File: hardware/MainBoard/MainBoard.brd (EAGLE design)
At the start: 90 x 56 mm, 265 parts, among them J1 CON-71741-2184-BOT, J2 CON-71741-2184-TOP, J3 CON-FTSH-105-01-L-DV-K, J4 CON-ZX62R-B-5P, J7 CON-RJ45-J0G-0007NL, J8 SWITCH-CJS-1200-1200, M1 MOUNT-HOLE3.3, M2 MOUNT-HOLE3.3, M3 MOUNT-HOLE3.3, M4 MOUNT-HOLE3.3, M5 FIDUCIAL1X2, M6 FIDUCIAL1X2, M7 FIDUCIAL1X2, M8 FIDUCIAL1X2, Q1 MMBT3904, SW1 SWITCH-ESWITCH-TL3340G, SW2 SWITCH-ESWITCH-TL3340G, U1 A2F500M3G-1FGG256, U2 MAX19706-T4877-4, U3 MAX19706-T4877-4, U4 USBLC6-2SC6, U5 FT232HL, U6 DP83848C-VBH48A, U7 93LC56BT-OT, U8 DS1818-10-SOT-23, X1 ECX-2236-200, X2 ECX-31B, X3 ASEM1-C, X5 ECX-42-120

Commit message: Minor cleanup and markup on schematic and board.
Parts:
- turned X5 to 90 degrees
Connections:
- net UXCSI: now also X5.3; no longer X5.1
- net UXCSO: now also X5.1; no longer X5.3
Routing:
- net DGND: track 148.5 -> 143.7 mm, vias 77 -> 75
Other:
- board text added: "Add more vias"
- board text added: "Consider adding thermal vias"
- board text added: "JTAG"
- board text added: "Reroute JTAG signals"
- board text added: "Star topology for ETH, USB, SF, AFEs?"
- board text removed: "Redraw JTAG signals"
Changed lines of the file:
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@@
 <setting verticaltext="up"/>
 </settings>
-<grid distance="100" unitdist="mil" unit="mil" style="lines" multiple="1" display="yes" altdistance="25" altunitdist="mil" altunit="mil"/>
+<grid distance="1" unitdist="mm" unit="mm" style="lines" multiple="1" display="yes" altdistance="0.25" altunitdist="mm" altunit="mm"/>
 <layers>
 <layer number="1" name="Top" color="4" fill="1" visible="yes" active="yes"/>
@@
 <layer number="14" name="Inner2" color="10" fill="6" visible="no" active="yes"/>
 <layer number="15" name="D3V3" color="4" fill="6" visible="no" active="yes"/>
-<layer number="16" name="Bottom" color="1" fill="1" visible="yes" active="yes"/>
+<layer number="16" name="Bottom" color="1" fill="1" visible="no" active="yes"/>
 <layer number="17" name="Pads" color="2" fill="1" visible="yes" active="yes"/>
 <layer number="18" name="Vias" color="2" fill="1" visible="yes" active="yes"/>
@@
 <rectangle x1="23" y1="6" x2="28" y2="8" layer="101"/>
 <rectangle x1="25" y1="32" x2="36" y2="42" layer="101"/>
-<text x="25" y="31" size="0.4064" layer="101">Should USB data signals run in the same layer?</text>
+<text x="20" y="31" size="0.8128" layer="101">Should USB data signals run in the same layer?</text>
 <rectangle x1="10" y1="25" x2="17" y2="33" layer="101"/>
-<text x="9" y="25" size="0.8128" layer="101" rot="R90">Redraw JTAG signals</text>
+<text x="8" y="24" size="0.8128" layer="101">Reroute JTAG signals</text>
 <text x="8.5" y="18.25" size="1.27" layer="21" font="vector" rot="R90">RESET</text>
 <text x="8.5" y="12.25" size="1.27" layer="21" font="vector" rot="R90">USER</text>
@@
 <text x="91.98" y="18.62" size="0.8128" layer="101" rot="R90">Should planes be closer to board edge?</text>
 <text x="-0.73" y="13.54" size="0.8128" layer="101" rot="R90">-moving the FTSH header 0.5 mm north</text>
+<text x="12" y="28.75" size="1.27" layer="21" font="vector" rot="R90">JTAG</text>
+<text x="40.54" y="17.73" size="0.8128" layer="101">Consider adding thermal vias</text>
+<rectangle x1="35" y1="16" x2="43" y2="24" layer="101"/>
+<rectangle x1="51" y1="16" x2="59" y2="24" layer="101"/>
+<text x="23.54" y="12.73" size="0.8128" layer="101">Add more vias</text>
+<text x="23.54" y="11.73" size="0.8128" layer="101">Star topology for ETH, USB, SF, AFEs?</text>
 </plain>
 <attributes>
@@
 <attribute name="TOLERANCE" value="1%" x="19" y="38.25" size="1.778" layer="28" rot="MR0" display="off"/>
 </element>
-<element name="X5" library="MainBoard" package="ECX-42" value="ECX-42-120" x="12.5" y="40.5" rot="R270">
-<attribute name="CLOAD" value="9 pF" x="12.5" y="40.5" size="1.778" layer="27" rot="R270" display="off"/>
-<attribute name="DIGI-KEY#" value="XC1608CT-ND" x="12.5" y="40.5" size="1.778" layer="27" rot="R270" display="off"/>
-<attribute name="FREQ-TOLERANCE" value="10 ppm" x="12.5" y="40.5" size="1.778" layer="27" rot="R270" display="off"/>
-<attribute name="MPN" value="ECS-120-9-42-CKM-TR" x="12.5" y="40.5" size="1.778" layer="27" rot="R270" display="off"/>
-<attribute name="FREQ-STABILITY" value="10 ppm" x="12.5" y="40.5" size="1.778" layer="27" rot="R270" display="off"/>
-<attribute name="MF" value="ECS" x="12.5" y="40.5" size="1.778" layer="27" rot="R270" display="off"/>
+<element name="X5" library="MainBoard" package="ECX-42" value="ECX-42-120" x="12.5" y="40.5" rot="R90">
+<attribute name="CLOAD" value="9 pF" x="12.5" y="40.5" size="1.778" layer="27" rot="R90" display="off"/>
+<attribute name="DIGI-KEY#" value="XC1608CT-ND" x="12.5" y="40.5" size="1.778" layer="27" rot="R90" display="off"/>
+<attribute name="FREQ-TOLERANCE" value="10 ppm" x="12.5" y="40.5" size="1.778" layer="27" rot="R90" display="off"/>
+<attribute name="MPN" value="ECS-120-9-42-CKM-TR" x="12.5" y="40.5" size="1.778" layer="27" rot="R90" display="off"/>
+<attribute name="FREQ-STABILITY" value="10 ppm" x="12.5" y="40.5" size="1.778" layer="27" rot="R90" display="off"/>
+<attribute name="MF" value="ECS" x="12.5" y="40.5" size="1.778" layer="27" rot="R90" display="off"/>
 </element>
 <element name="C71" library="MainBoard" package="C0402" value="10pF" x="12.5" y="37" rot="R180"/>
@@
 <contactref element="C103" pad="2"/>
 <contactref element="C104" pad="2"/>
-<contactref element="C72" pad="2"/>
-<contactref element="C71" pad="2"/>
 <contactref element="C105" pad="2"/>
 <contactref element="C106" pad="2"/>
@@
 <vertex x="87" y="53"/>
 </polygon>
-<wire x1="10" y1="39.85" x2="10" y2="39" width="0.3048" layer="1"/>
-<via x="10" y="39" extent="1-16" drill="0.2032"/>
-<wire x1="11.7" y1="39" x2="10" y2="39" width="0.3048" layer="1"/>
-<wire x1="11.85" y1="37" x2="11" y2="37" width="0.3048" layer="1"/>
-<via x="11" y="37" extent="1-16" drill="0.2032"/>
-<wire x1="13.3" y1="42" x2="14.75" y2="42" width="0.3048" layer="1"/>
 <via x="14.75" y="42" extent="1-16" drill="0.2032"/>
 <wire x1="19.65" y1="38.25" x2="20.75" y2="38.25" width="0.3048" layer="16"/>
@@
 <wire x1="51.25" y1="38" x2="51" y2="38" width="0.1524" layer="16"/>
 <wire x1="50.65" y1="38" x2="51" y2="38" width="0.1524" layer="16"/>
+<contactref element="C72" pad="2"/>
+<contactref element="C71" pad="2"/>
 </signal>
 <signal name="D1V5">
@@
 </signal>
 <signal name="UXCSI">
-<contactref element="X5" pad="1"/>
 <contactref element="U5" pad="1"/>
-<contactref element="C72" pad="1"/>
-<wire x1="11.7" y1="42" x2="11.7" y2="41.8" width="0.1524" layer="1"/>
 <wire x1="11.7" y1="41.8" x2="12.75" y2="40.75" width="0.3048" layer="1"/>
 <wire x1="12.75" y1="40.75" x2="15.8" y2="40.75" width="0.3048" layer="1"/>
-<wire x1="11.7" y1="42" x2="10.85" y2="42" width="0.3048" layer="1"/>
-<wire x1="10.85" y1="42" x2="10" y2="41.15" width="0.3048" layer="1"/>
+<contactref element="X5" pad="3"/>
+<wire x1="11.7" y1="41.8" x2="11.7" y2="42" width="0.3048" layer="1"/>
+<contactref element="C72" pad="1"/>
+<wire x1="10" y1="41.15" x2="10.85" y2="42" width="0.3048" layer="1"/>
+<wire x1="10.85" y1="42" x2="11.25" y2="42" width="0.3048" layer="1"/>
+<wire x1="11.7" y1="41.8" x2="11.45" y2="41.8" width="0.3048" layer="1"/>
+<wire x1="11.45" y1="41.8" x2="11.25" y2="42" width="0.3048" layer="1"/>
 </signal>
 <signal name="UXCSO">
 <contactref element="U5" pad="2"/>
-<contactref element="X5" pad="3"/>
-<contactref element="C71" pad="1"/>
-<wire x1="13.3" y1="39" x2="14.55" y2="40.25" width="0.3048" layer="1"/>
 <wire x1="14.55" y1="40.25" x2="15.8" y2="40.25" width="0.3048" layer="1"/>
-<wire x1="13.3" y1="39" x2="13.3" y2="37.15" width="0.3048" layer="1"/>
-<wire x1="13.3" y1="37.15" x2="13.15" y2="37" width="0.3048" layer="1"/>
+<contactref element="X5" pad="1"/>
+<wire x1="14.55" y1="40.25" x2="13.3" y2="39" width="0.3048" layer="1"/>
+<contactref element="C71" pad="1"/>
+<wire x1="13.15" y1="37" x2="13.3" y2="37.15" width="0.3048" layer="1"/>
+<wire x1="13.3" y1="37.15" x2="13.3" y2="39" width="0.3048" layer="1"/>
 </signal>
 <signal name="EECS">

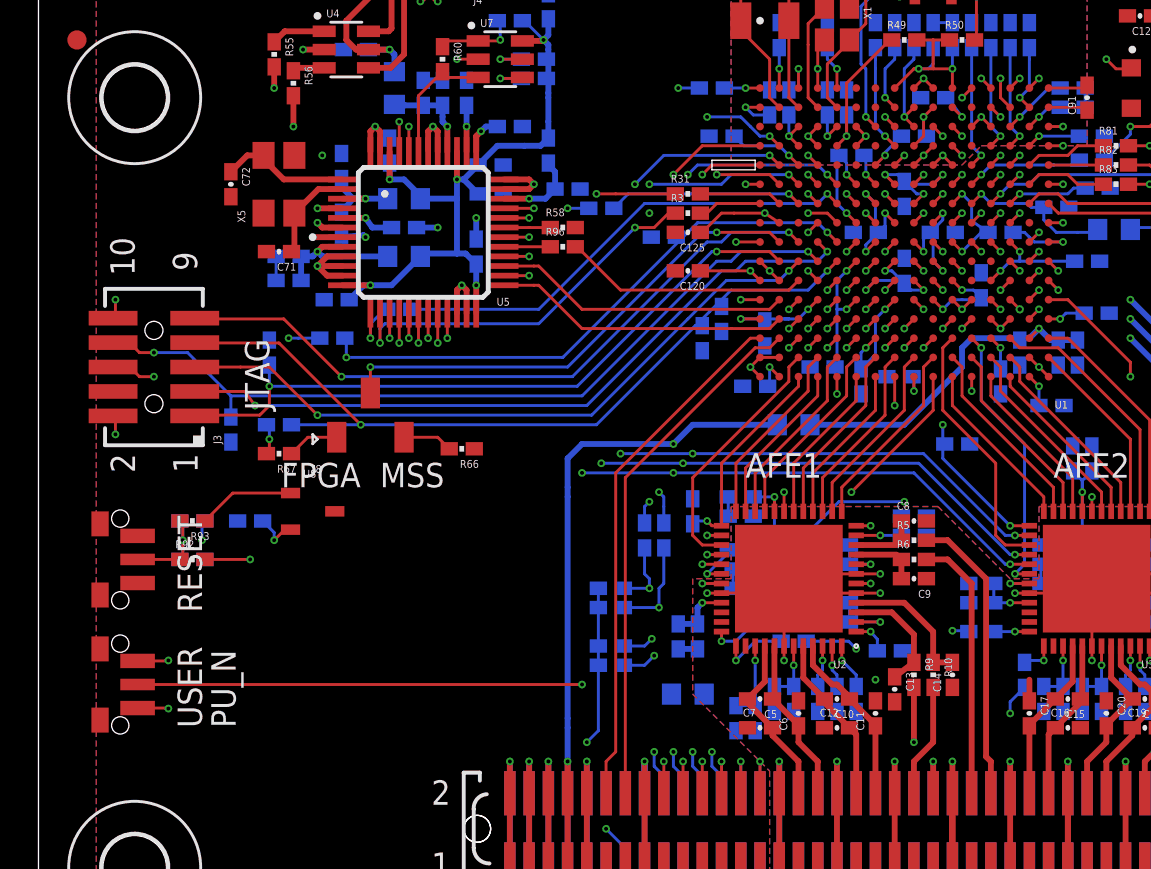
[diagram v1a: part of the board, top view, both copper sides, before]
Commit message: 
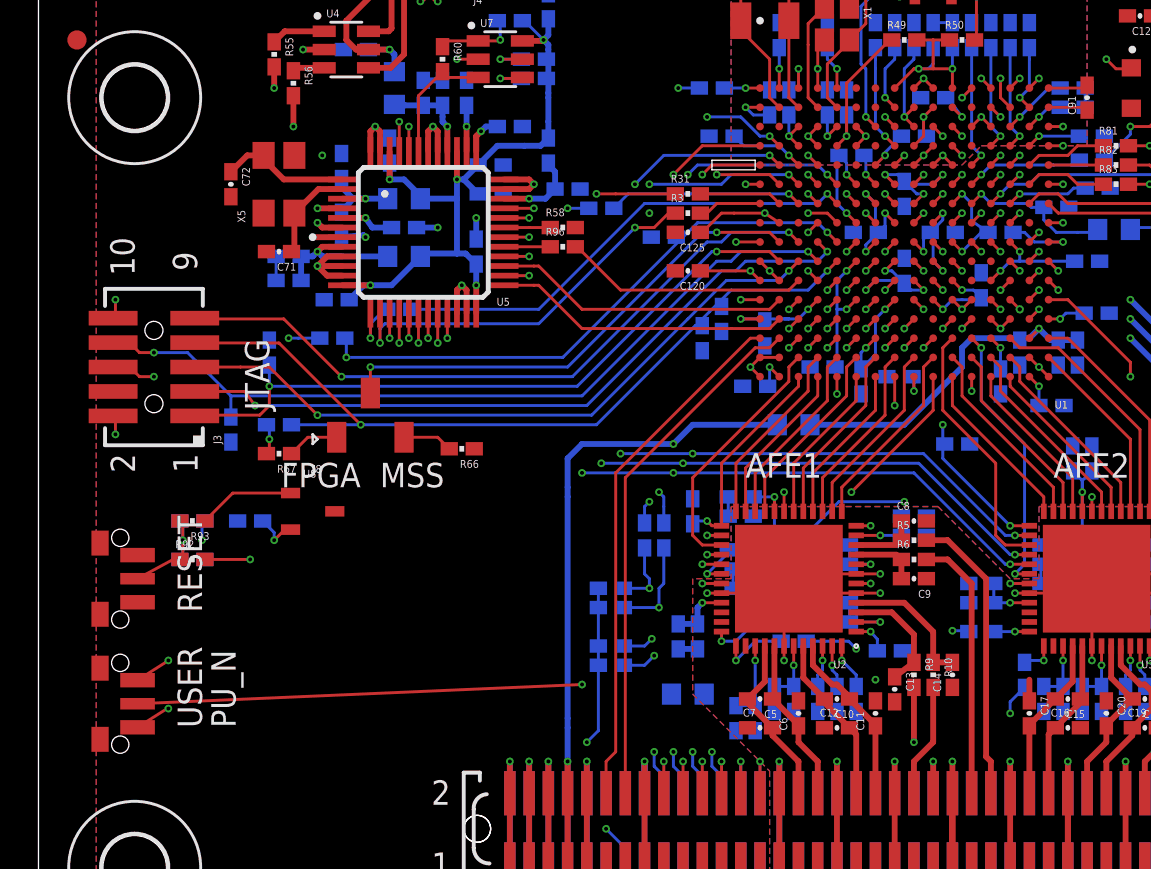
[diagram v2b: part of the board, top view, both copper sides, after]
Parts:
- moved SW1 1.00 mm to (2.75, 20.0)
- moved SW2 1.00 mm to (2.75, 13.5)
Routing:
- net DGND: track 143.7 -> 144.3 mm
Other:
- board text added: "1mm closer to board edge?"
- board text removed: "-moving the FTSH header 0.5 mm north"
- board text removed: "-using a larger switch (e.g. KSC421 V30 ACT2.95 LFS)"
- board text removed: "Add more vias"
- board text removed: "Consider adding thermal vias"
- board text removed: "Consider:"
- board text removed: "Reroute JTAG signals"
- board text removed: "Should USB data signals run in the same layer?"
- board text removed: "Should planes be closer to board edge?"
- board text removed: "Star topology for ETH, USB, SF, AFEs?"
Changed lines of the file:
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@@
 <layer number="1" name="Top" color="4" fill="1" visible="yes" active="yes"/>
 <layer number="2" name="GND" color="1" fill="3" visible="no" active="yes"/>
-<layer number="3" name="Inner1" color="13" fill="3" visible="no" active="yes"/>
-<layer number="14" name="Inner2" color="10" fill="6" visible="no" active="yes"/>
+<layer number="3" name="Inner1" color="13" fill="3" visible="yes" active="yes"/>
+<layer number="14" name="Inner2" color="10" fill="6" visible="yes" active="yes"/>
 <layer number="15" name="D3V3" color="4" fill="6" visible="no" active="yes"/>
 <layer number="16" name="Bottom" color="1" fill="1" visible="no" active="yes"/>
@@
 <layer number="27" name="tValues" color="7" fill="1" visible="no" active="yes"/>
 <layer number="28" name="bValues" color="7" fill="1" visible="no" active="yes"/>
-<layer number="29" name="tStop" color="7" fill="3" visible="no" active="yes"/>
+<layer number="29" name="tStop" color="7" fill="3" visible="yes" active="yes"/>
 <layer number="30" name="bStop" color="7" fill="6" visible="no" active="yes"/>
-<layer number="31" name="tCream" color="7" fill="4" visible="no" active="yes"/>
+<layer number="31" name="tCream" color="7" fill="4" visible="yes" active="yes"/>
 <layer number="32" name="bCream" color="7" fill="5" visible="no" active="yes"/>
 <layer number="33" name="tFinish" color="6" fill="3" visible="no" active="yes"/>
@@
 <rectangle x1="62" y1="10" x2="66" y2="11" layer="101"/>
 <rectangle x1="28" y1="2" x2="31" y2="8" layer="116"/>
-<text x="-3" y="13.54" size="0.8128" layer="101" rot="R90">Consider:</text>
-<text x="-2" y="13.54" size="0.8128" layer="101" rot="R90">-using a larger switch (e.g. KSC421 V30 ACT2.95 LFS)</text>
 <rectangle x1="62" y1="6" x2="67" y2="8" layer="101"/>
 <rectangle x1="23" y1="6" x2="28" y2="8" layer="101"/>
-<rectangle x1="25" y1="32" x2="36" y2="42" layer="101"/>
-<text x="20" y="31" size="0.8128" layer="101">Should USB data signals run in the same layer?</text>
-<rectangle x1="10" y1="25" x2="17" y2="33" layer="101"/>
-<text x="8" y="24" size="0.8128" layer="101">Reroute JTAG signals</text>
+<rectangle x1="14" y1="24" x2="21" y2="32" layer="101"/>
 <text x="8.5" y="18.25" size="1.27" layer="21" font="vector" rot="R90">RESET</text>
 <text x="8.5" y="12.25" size="1.27" layer="21" font="vector" rot="R90">USER</text>
@@
 <text x="36.75" y="25.25" size="1.27" layer="21" font="vector">AFE1</text>
 <text x="52.75" y="25.25" size="1.27" layer="21" font="vector">AFE2</text>
-<text x="91.98" y="18.62" size="0.8128" layer="101" rot="R90">Should planes be closer to board edge?</text>
-<text x="-0.73" y="13.54" size="0.8128" layer="101" rot="R90">-moving the FTSH header 0.5 mm north</text>
+<text x="91.98" y="18.62" size="0.8128" layer="101" rot="R90">1mm closer to board edge?</text>
 <text x="12" y="28.75" size="1.27" layer="21" font="vector" rot="R90">JTAG</text>
-<text x="40.54" y="17.73" size="0.8128" layer="101">Consider adding thermal vias</text>
 <rectangle x1="35" y1="16" x2="43" y2="24" layer="101"/>
 <rectangle x1="51" y1="16" x2="59" y2="24" layer="101"/>
-<text x="23.54" y="12.73" size="0.8128" layer="101">Add more vias</text>
-<text x="23.54" y="11.73" size="0.8128" layer="101">Star topology for ETH, USB, SF, AFEs?</text>
+<rectangle x1="12" y1="44" x2="19" y2="52" layer="101"/>
+<rectangle x1="3" y1="12" x2="10" y2="20" layer="101"/>
 </plain>
 <attributes>
@@
 <attribute name="DNP" value="on" x="33.75" y="14" size="1.778" layer="28" rot="MR180" display="off"/>
 </element>
-<element name="SW1" library="MainBoard" package="TL3340" value="SWITCH-ESWITCH-TL3340G" x="2.75" y="21" rot="R270"/>
-<element name="SW2" library="MainBoard" package="TL3340" value="SWITCH-ESWITCH-TL3340G" x="2.75" y="14.5" rot="R270"/>
+<element name="SW1" library="MainBoard" package="TL3340" value="SWITCH-ESWITCH-TL3340G" x="2.75" y="20" rot="R270"/>
+<element name="SW2" library="MainBoard" package="TL3340" value="SWITCH-ESWITCH-TL3340G" x="2.75" y="13.5" rot="R270"/>
 <element name="C148" library="MainBoard" package="C0402" value="1000pF" x="60.5" y="47.5" rot="MR0">
 <attribute name="PAGE3" value="Clock and Reset" x="60.5" y="47.5" size="1.778" layer="28" rot="MR0" display="off"/>
@@
 <contactref element="SW2" pad="1"/>
 <contactref element="SW2" pad="3"/>
-<wire x1="5.15" y1="15.725" x2="6.725" y2="15.725" width="0.1524" layer="1"/>
+<wire x1="5.15" y1="14.725" x2="6.725" y2="15.725" width="0.1524" layer="1"/>
 <wire x1="6.725" y1="15.725" x2="6.75" y2="15.75" width="0.1524" layer="1"/>
 <via x="6.75" y="15.75" extent="1-16" drill="0.2032"/>
-<wire x1="5.15" y1="13.275" x2="6.725" y2="13.275" width="0.1524" layer="1"/>
+<wire x1="5.15" y1="12.275" x2="6.725" y2="13.275" width="0.1524" layer="1"/>
 <wire x1="6.725" y1="13.275" x2="6.75" y2="13.25" width="0.1524" layer="1"/>
 <via x="6.75" y="13.25" extent="1-16" drill="0.2032"/>
@@
 <via x="34.75" y="44" extent="1-16" drill="0.2032"/>
 <wire x1="38" y1="43" x2="37.5" y2="43" width="0.1524" layer="16"/>
-<wire x1="37.5" y1="43" x2="37" y2="43.5" width="0.1524" layer="16"/>
-<wire x1="37" y1="43.5" x2="36.5" y2="44" width="0.1524" layer="16"/>
+<wire x1="37.5" y1="43" x2="36.5" y2="44" width="0.1524" layer="16"/>
 <wire x1="36.5" y1="44" x2="34.75" y2="44" width="0.1524" layer="16"/>
 <via x="31.75" y="39" extent="1-16" drill="0.2032"/>
 <wire x1="53.25" y1="37.5" x2="51.75" y2="37.5" width="0.1524" layer="16"/>
-<wire x1="51.75" y1="37.5" x2="51.5" y2="37.75" width="0.1524" layer="16"/>
-<wire x1="51.5" y1="37.75" x2="51.25" y2="38" width="0.1524" layer="16"/>
-<wire x1="51.25" y1="38" x2="51" y2="38" width="0.1524" layer="16"/>
-<wire x1="50.65" y1="38" x2="51" y2="38" width="0.1524" layer="16"/>
+<wire x1="51.75" y1="37.5" x2="51.25" y2="38" width="0.1524" layer="16"/>
+<wire x1="50.65" y1="38" x2="51.25" y2="38" width="0.1524" layer="16"/>
 <contactref element="C72" pad="2"/>
 <contactref element="C71" pad="2"/>
@@
 <contactref element="R93" pad="2"/>
 <contactref element="SW1" pad="2"/>
-<wire x1="5.15" y1="21" x2="7" y2="21" width="0.1524" layer="1"/>
+<wire x1="5.15" y1="20" x2="7" y2="21" width="0.1524" layer="1"/>
 <wire x1="7.35" y1="21" x2="7.5" y2="21.15" width="0.1524" layer="1"/>
 <wire x1="7.5" y1="21.15" x2="7.5" y2="22" width="0.1524" layer="1"/>
@@
 <wire x1="36.75" y1="45.5" x2="35.25" y2="45.5" width="0.1524" layer="14"/>
 <contactref element="SW2" pad="2"/>
-<wire x1="5.15" y1="14.5" x2="28.25" y2="14.5" width="0.1524" layer="1"/>
+<wire x1="5.15" y1="13.5" x2="28.25" y2="14.5" width="0.1524" layer="1"/>
 <via x="28.25" y="14.5" extent="1-16" drill="0.2032"/>
 </signal>
@@
 </signal>
 </signals>
-<errors>
-</errors>
 </board>
 </drawing>
